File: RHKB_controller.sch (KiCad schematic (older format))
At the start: 7 parts

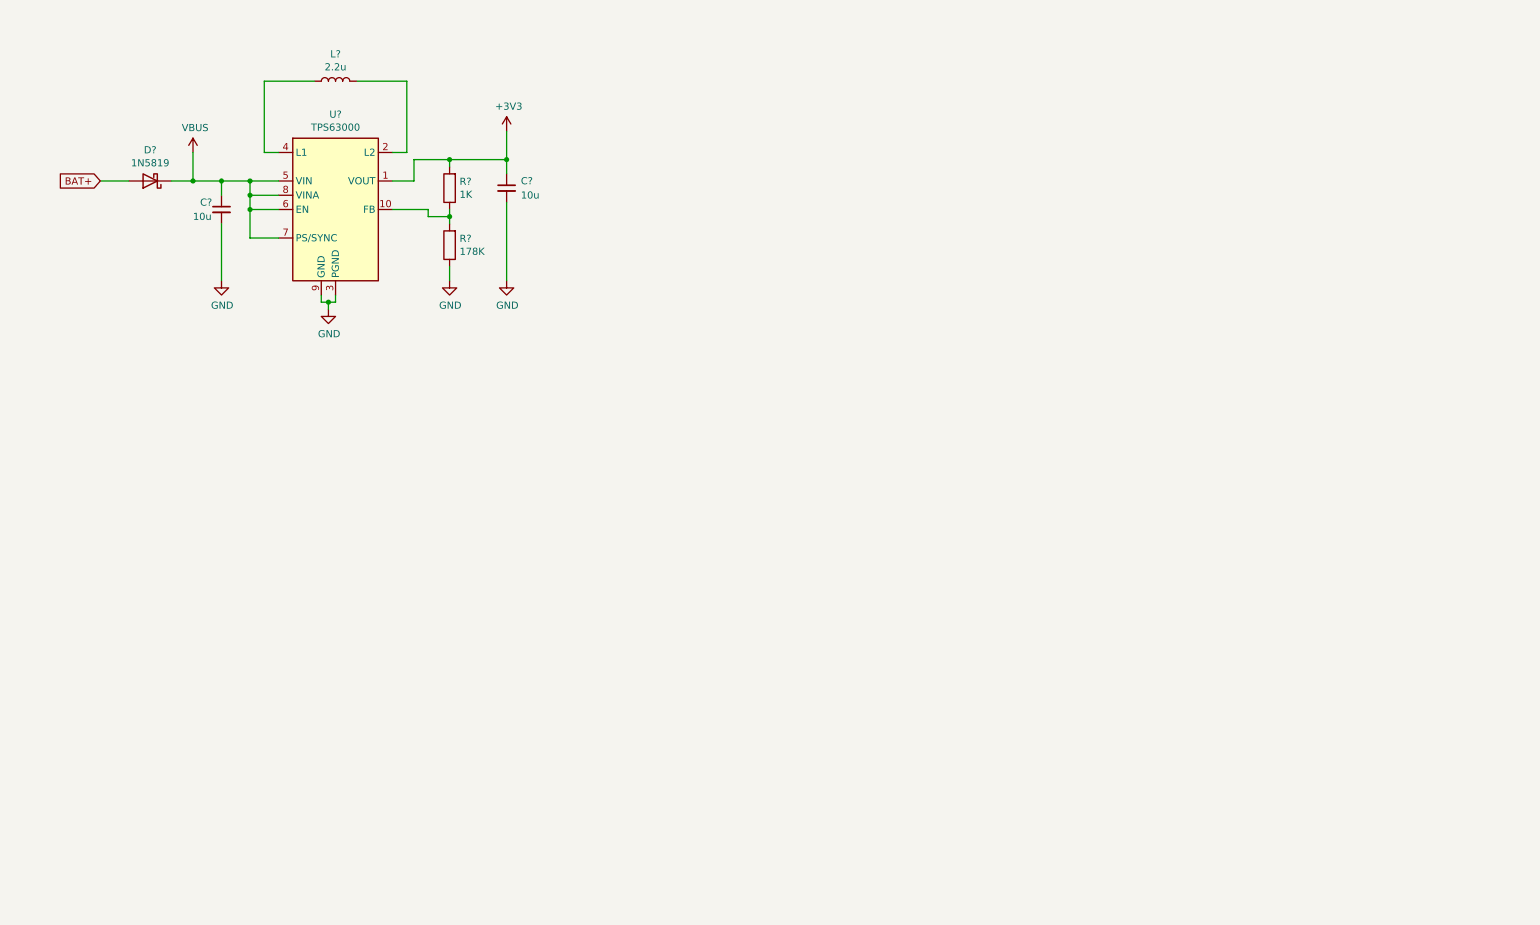
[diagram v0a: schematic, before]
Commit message: Add HHKB connectors and battery management modules
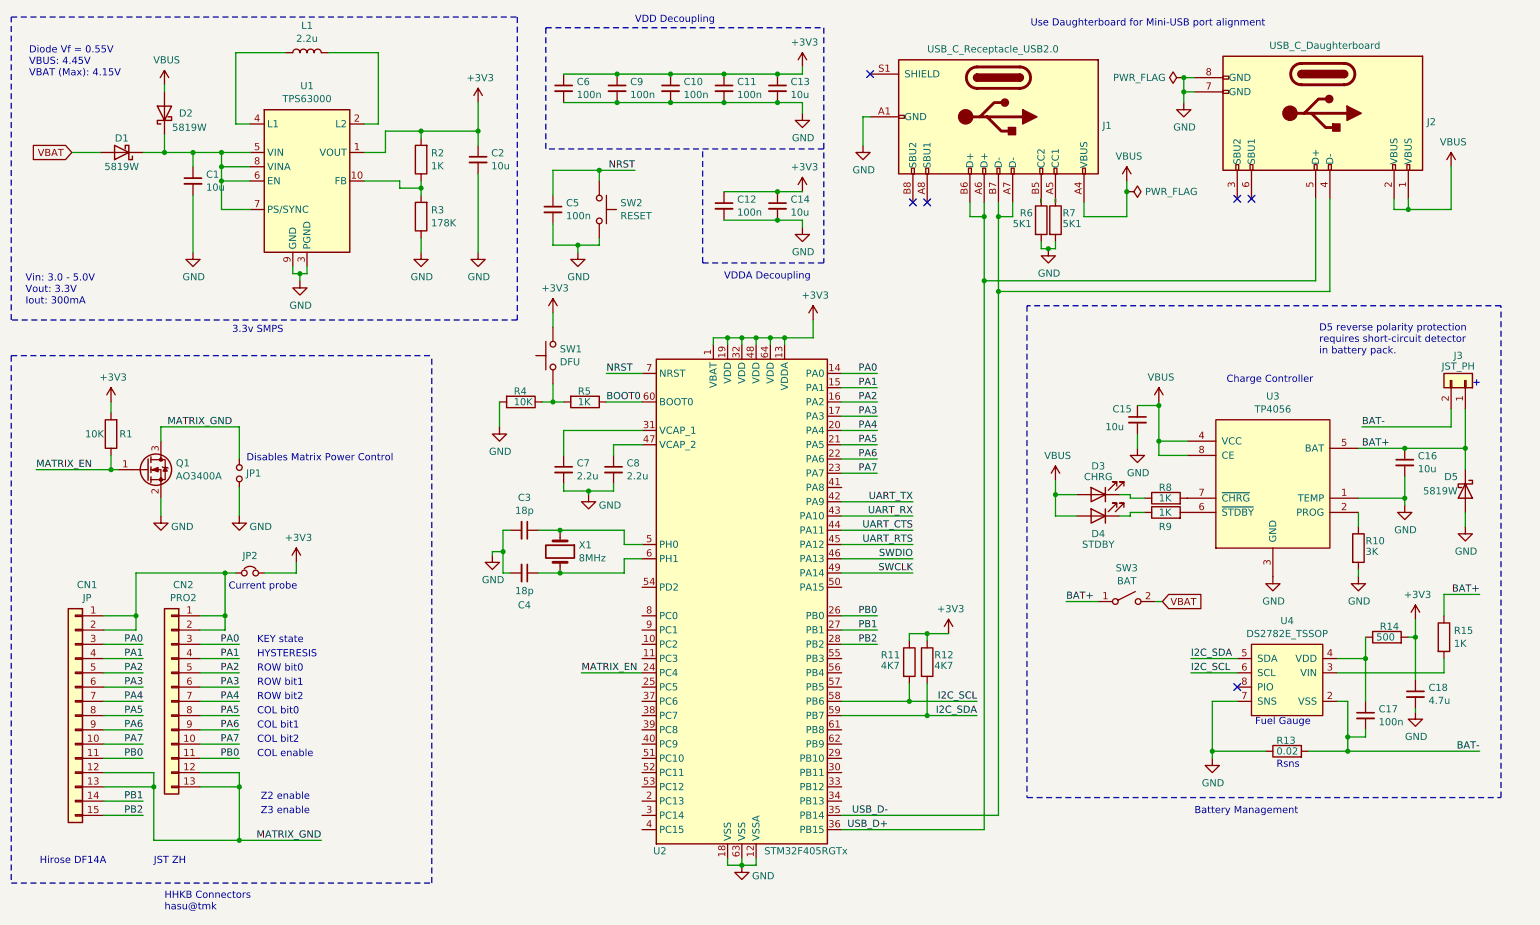
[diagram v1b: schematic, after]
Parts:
- removed C? (x2): 10u, symbol Device:C_Small
- removed D?: 1N5819, Diode_THT:D_DO-41_SOD81_P10.16mm_Horizontal, symbol Diode:1N5819
- removed L?: 2.2u, symbol Device:L
- removed R?: 1K, symbol Device:R
- removed R?: 178K, symbol Device:R
- removed U?: TPS63000, Package_SON:Texas_DRC0010J_ThermalVias, symbol Regulator_Switching:TPS63000
- added C1, C13, C14, C15, C16, C2: 10u, Capacitor_SMD:C_0603_1608Metric, symbol Device:C_Small
- added C10, C11, C12, C17, C5, C6, C9: 100n, Resistor_SMD:R_0402_1005Metric, symbol Device:C_Small
- added C18: 4.7u, Capacitor_SMD:C_0603_1608Metric, symbol Device:C_Small
- added C3, C4: 18p, Capacitor_SMD:C_0402_1005Metric, symbol Device:C_Small
- added C7, C8: 2.2u, Capacitor_SMD:C_0402_1005Metric, symbol Device:C_Small
- added CN1: JP, symbol Connector_Generic:Conn_01x15
- added CN2: PRO2, symbol Connector_Generic:Conn_01x13
- added D1, D2, D5: 5819W, Diode_SMD:D_SOD-123, symbol Diode:1N5819
- added D3: CHRG, LED_SMD:LED_0603_1608Metric, symbol Device:LED
- added D4: STDBY, LED_SMD:LED_0603_1608Metric, symbol Device:LED
- added J1: USB_C_Receptacle_USB2.0, symbol Connector:USB_C_Receptacle_USB2.0
- added J2: USB_C_Daughterboard, symbol Connector_USB:USB_C_Daughterboard
- added J3: JST_PH, symbol Connector_Generic:Conn_01x02
- added JP1: Matrix_Current, symbol Device:Jumper_NO_Small
- added JP2: Matrix_Current, symbol Device:Jumper_NC_Small
- added L1: 2.2u, Inductor_SMD:L_0805_2012Metric, symbol Device:L
- added Q1: AO3400A, symbol Device:Q_NMOS_GSD
- added R1, R4: 10K, symbol Device:R
- added R10: 3K, symbol Device:R
- added R11, R12: 4K7, symbol Device:R
- added R13: 0.02, symbol Device:R
- added R14: 500, symbol Device:R
- added R15, R2, R5, R8, R9: 1K, symbol Device:R
- added R3: 178K, symbol Device:R
- added R6, R7: 5K1, symbol Device:R
- added SW1: DFU, symbol Switch:SW_Push
- added SW2: RESET, symbol Switch:SW_Push
- added SW3: BAT, symbol Switch:SW_SPST
- added U1: TPS63000, Package_SON:Texas_DRC0010J_ThermalVias, symbol Regulator_Switching:TPS63000
- added U2: STM32F405RGTx, Package_QFP:LQFP-64_10x10mm_P0.5mm, symbol MCU_ST_STM32F4:STM32F405RGTx
- added U3: TP4056, symbol Charge_Controller:TP4056
- added U4: DS2782E_TSSOP, symbol Charge_Controller:DS2782E_TSSOP
- added X1: 8MHz, Crystal:Crystal_SMD_5032-2Pin_5.0x3.2mm, symbol Device:Crystal
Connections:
- net +3V3: now also C10.1, C11.1, C12.1, C13.1, C14.1, C18.1, C2.1, C6.1, C9.1, JP2.2, R1.2, R11.1, R12.1, R14.2, R2.2, SW1.2, U1.1 (VOUT), U2.1 (VBAT), U2.13 (VDDA), U2.19 (VDD), U2.32 (VDD), U2.48 (VDD), U2.64 (VDD)
- net BAT+: now also C16.1, D5.1 (K), J3.1 (Pin_1), R15.1, SW3.1 (A), U3.5 (BAT)
- net GND: now also C1.2, C10.2, C11.2, C12.2, C13.2, C14.2, C15.2, C16.2, C18.2, C2.2, C3.2, C4.2, C5.2, C6.2, C7.2, C8.2, C9.2, D5.2 (A), J1.A1 (GND), J1.A12 (GND), J1.B1 (GND), J1.B12 (GND), J2.7 (GND), J2.8 (GND), JP1.2, Q1.2 (S), R10.2, R13.1, R3.1, R4.2, R6.2, R7.2, SW2.2, U1.11 (PGND), U1.3 (PGND), U1.9 (GND), U2.12 (VSSA), U2.18 (VSS), U2.63 (VSS), U3.1 (TEMP), U3.3 (GND), U4.7 (SNS)
- net VBUS: now also C15.1, D2.2 (A), D3.2 (A), D4.2 (A), J1.A4 (VBUS), J1.A9 (VBUS), J1.B4 (VBUS), J1.B9 (VBUS), J2.1 (VBUS), J2.2 (VBUS), U3.4 (VCC), U3.8 (CE)
- new net: C8.1, U2.47 (VCAP_2)
- new net: C1.1, D1.1 (K), D2.1 (K), U1.5 (VIN), U1.6 (EN), U1.7 (PS/SYNC), U1.8 (VINA)
- new net: C7.1, U2.31 (VCAP_1)
- new net: C3.1, U2.5 (PH0), X1.1
- new net: C4.1, U2.6 (PH1), X1.2
- new net: J1.B5 (CC2), R6.1
- new net: J1.A5 (CC1), R7.1
- new net: R2.1, R3.2, U1.10 (FB)
- new net: L1.2, U1.2 (L2)
- new net: L1.1, U1.4 (L1)
- new net: R15.2, U4.3 (VIN)
- new net: C17.1, R14.1, U4.4 (VDD)
- new net: R4.1, R5.2, SW1.1
- new net: CN1.1 (Pin_1), CN1.2 (Pin_2), CN2.1 (Pin_1), CN2.2 (Pin_2), JP2.1
- new net: R10.1, U3.2 (PROG)
- new net: R9.2, U3.6 (~STDBY)
- new net: R8.2, U3.7 (~CHRG)
- new net: D3.1 (K), R8.1
- new net: D4.1 (K), R9.1
- new net BAT-: C17.2, J3.2 (Pin_2), R13.2, U4.2 (VSS)
- new net BOOT0: R5.1, U2.60 (BOOT0)
- new net I2C_SCL: R11.2, U2.58 (PB6), U4.6 (SCL)
- new net I2C_SDA: R12.2, U2.59 (PB7), U4.5 (SDA)
- new net MATRIX_EN: Q1.1 (G), R1.1, U2.24 (PC4)
- new net MATRIX_GND: CN1.12 (Pin_12), CN1.13 (Pin_13), CN2.12 (Pin_12), CN2.13 (Pin_13), JP1.1, Q1.3 (D)
- new net NRST: C5.1, SW2.1, U2.7 (NRST)
- new net PA0: CN1.3 (Pin_3), CN2.3 (Pin_3), U2.14 (PA0)
- new net PA1: CN1.4 (Pin_4), CN2.4 (Pin_4), U2.15 (PA1)
- new net PA2: CN1.5 (Pin_5), CN2.5 (Pin_5), U2.16 (PA2)
- new net PA3: CN1.6 (Pin_6), CN2.6 (Pin_6), U2.17 (PA3)
- new net PA4: CN1.7 (Pin_7), CN2.7 (Pin_7), U2.20 (PA4)
- new net PA5: CN1.8 (Pin_8), CN2.8 (Pin_8), U2.21 (PA5)
- new net PA6: CN1.9 (Pin_9), CN2.9 (Pin_9), U2.22 (PA6)
- new net PA7: CN1.10 (Pin_10), CN2.10 (Pin_10), U2.23 (PA7)
- new net PB0: CN1.11 (Pin_11), CN2.11 (Pin_11), U2.26 (PB0)
- new net PB1: CN1.14 (Pin_14), U2.27 (PB1)
- new net PB2: CN1.15 (Pin_15), U2.28 (PB2)
- new net SWCLK: U2.49 (PA14)
- new net SWDIO: U2.46 (PA13)
- new net UART_CTS: U2.44 (PA11)
- new net UART_RTS: U2.45 (PA12)
- new net UART_RX: U2.43 (PA10)
- new net UART_TX: U2.42 (PA9)
- new net USB_D+: J1.A6 (D+), J1.B6 (D+), J2.5 (D+), U2.36 (PB15)
- new net USB_D-: J1.A7 (D-), J1.B7 (D-), J2.4 (D-), U2.35 (PB14)
- new net VBAT: D1.2 (A), SW3.2 (B)
- no-connect marks 0 -> 6
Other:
- note added: "+"
- note added: "3.3v SMPS"
- note added: "Battery Management"
- note added: "COL bit0"
- note added: "COL bit1"
- note added: "COL bit2"
- note added: "COL enable"
- note added: "Charge Controller"
- note added: "Current probe"
- note added: "D5 reverse polarity protection\nrequires short-circuit detector\nin battery pack."
- note added: "Diode Vf = 0.55V\nVBUS: 4.45V\nVBAT (Max): 4.15V"
- note added: "Disables Matrix Power Control"
- note added: "Fuel Gauge"
- note added: "HHKB Connectors\nhasu@tmk"
- note added: "HYSTERESIS"
- note added: "Hirose DF14A"
- note added: "JST ZH"
- note added: "KEY state"
- note added: "ROW bit0"
- note added: "ROW bit1"
- note added: "ROW bit2"
- note added: "Rsns"
- note added: "Use Daughterboard for Mini-USB port alignment"
- note added: "VDD Decoupling"
- note added: "VDDA Decoupling"
- note added: "Vin: 3.0 - 5.0V\nVout: 3.3V\nIout: 300mA"
- note added: "Z2 enable"
- note added: "Z3 enable"
